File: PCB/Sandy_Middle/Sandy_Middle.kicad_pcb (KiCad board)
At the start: 2 copper layers, 285 x 75.2 mm, 134 parts, among them J1 Conn_02x02_Top_Bottom, J2 Conn_02x02_Top_Bottom, J3 Conn_02x02_Top_Bottom

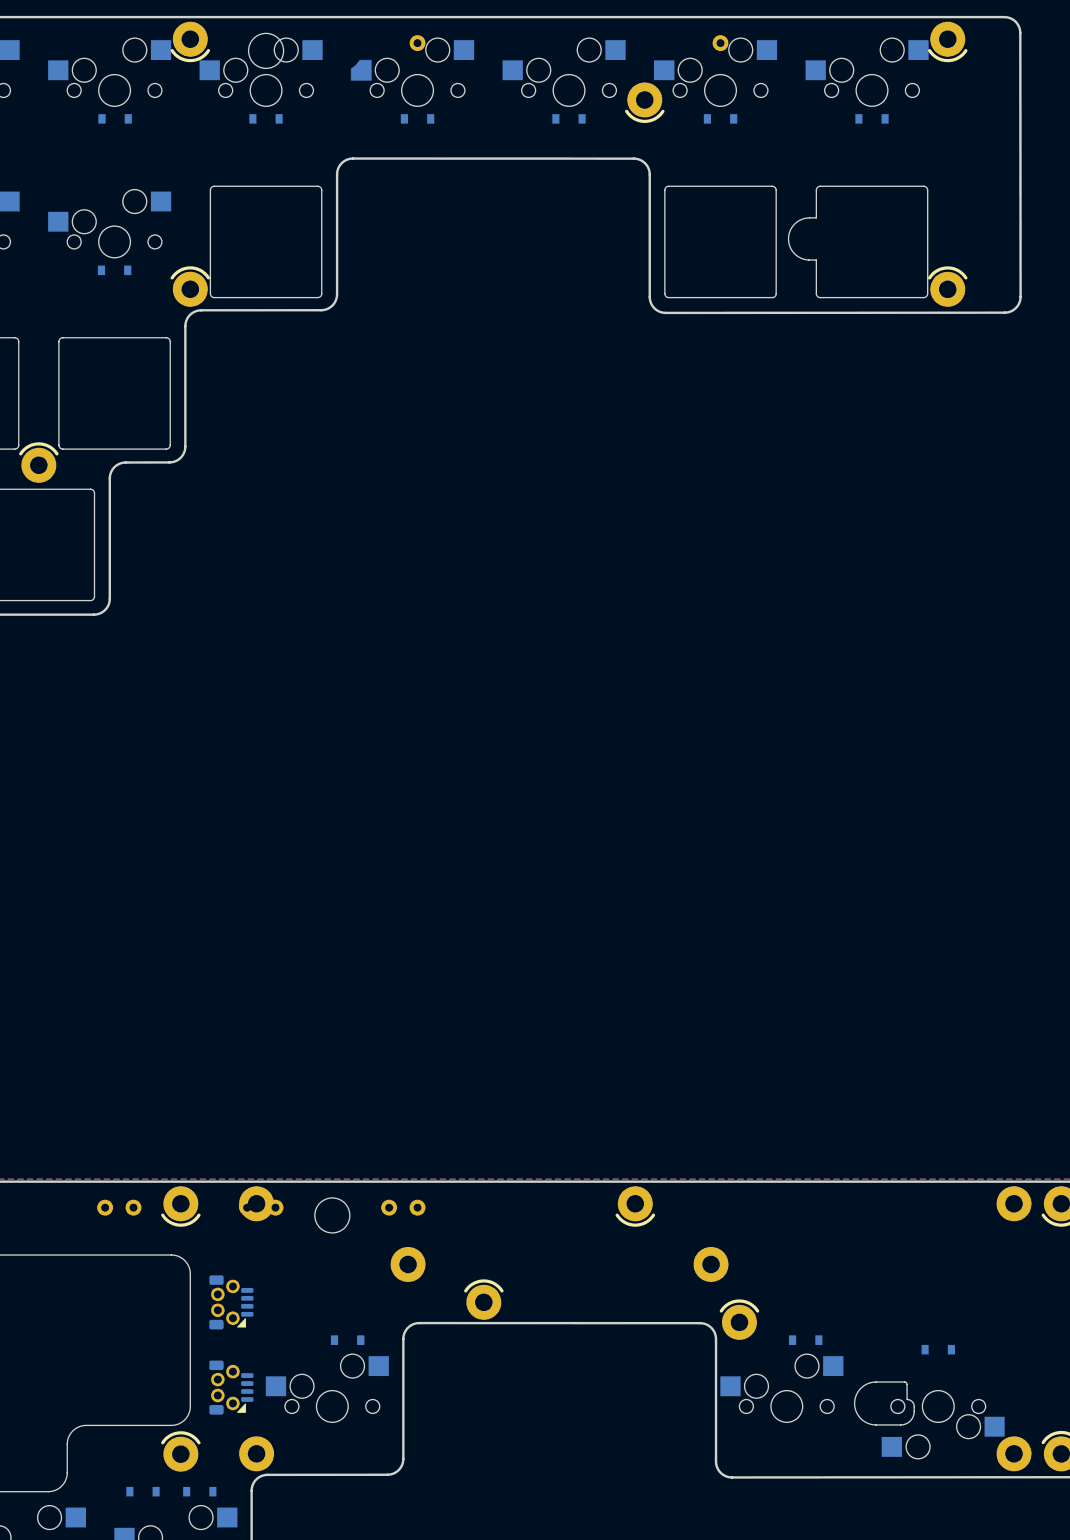
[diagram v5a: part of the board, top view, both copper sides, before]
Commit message: スイッチの配置イメージをDN0040レイアウトに変更
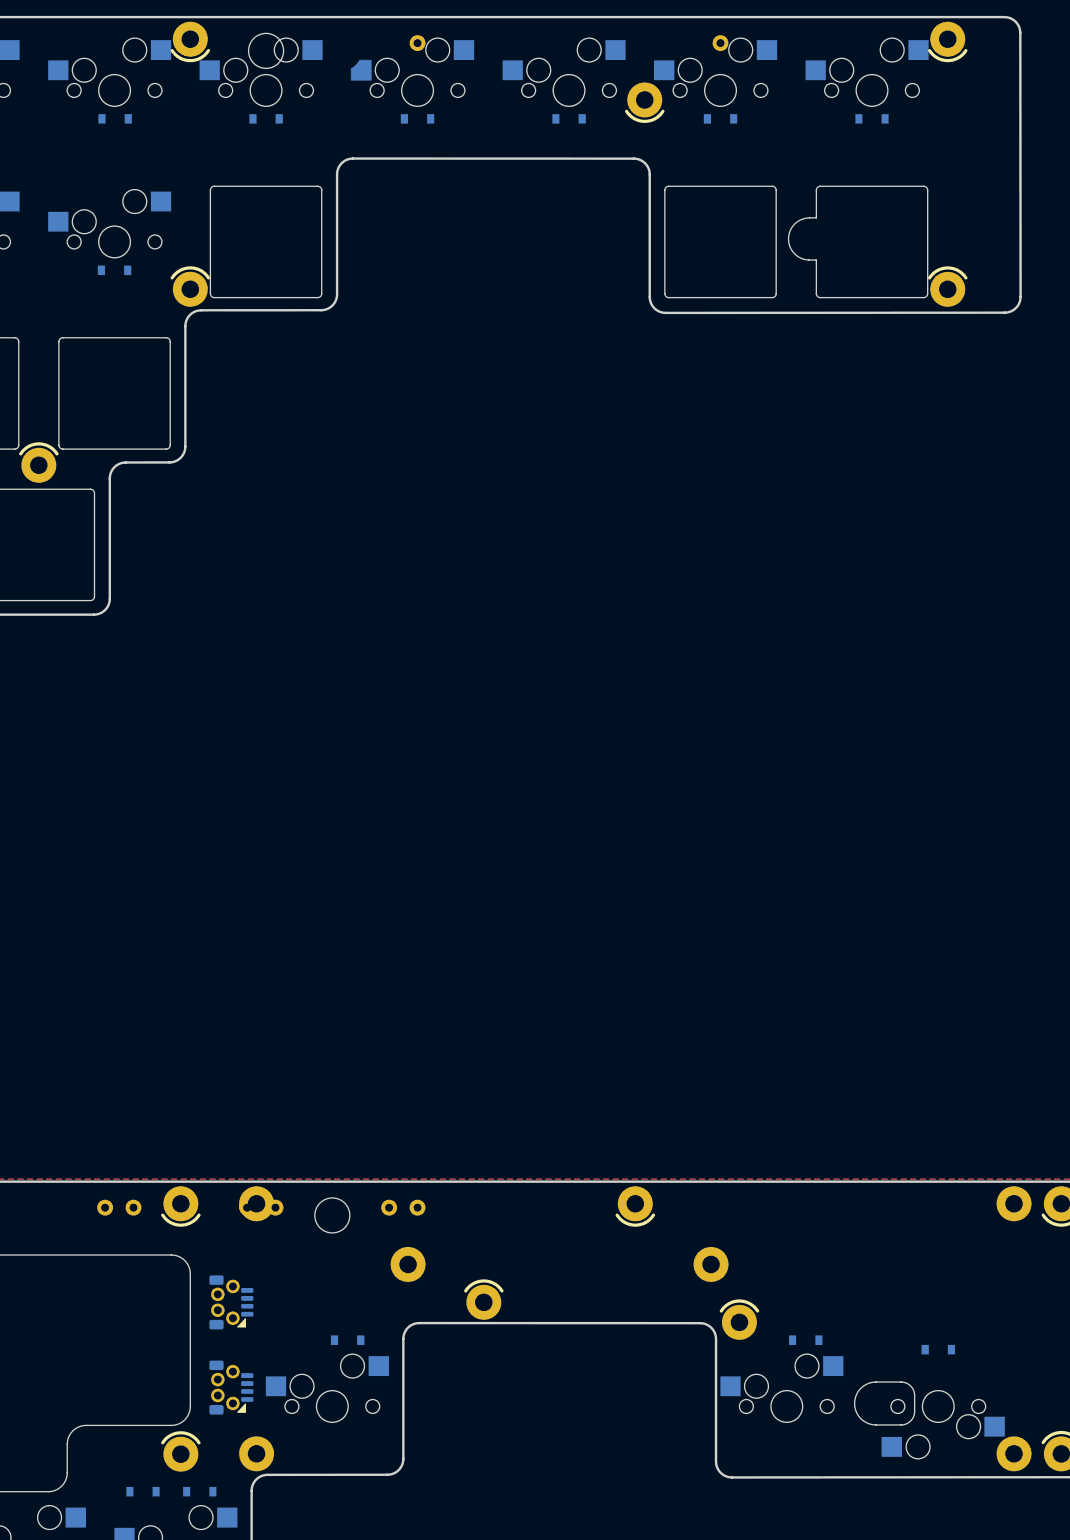
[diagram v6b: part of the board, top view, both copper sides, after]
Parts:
- Cutout1: footprint locallib:60_Outline-Sandy-Mid7-narrow-bottom-small-right-hole -> locallib:60_Outline-Sandy-DN0040-Mid
- REF**: footprint locallib:60_Outline-Sandy-Top-NoSwImage-WithHole2-ECO1 -> locallib:60_Outline-Sandy-DN0040-Top-NoSwImage-WithHole2-ECO1

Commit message: ネジ穴と接続するピンを調整中
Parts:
- removed ?: , clipboard:1d23b097-72e0-487b-bec7-a328ee8b6ed7
- removed the D1 at (31.8, -112.3)
- removed D10 (x2), D14, D16, D17, D18, D19, D8 (x2): D, locallib:D_SOD-123_Emphasized_Direction_Line
- removed the D11 at (222.3, -112.3)
- removed the D12 at (241.3, -112.3)
- removed the D13 at (260.4, -112.3)
- removed the D2 at (50.8, -112.3)
- removed the D3 at (69.9, -112.3)
- removed the D4 at (88.9, -112.3)
- removed the D5 at (108.0, -112.3)
- removed the D6 at (127.0, -112.3)
- removed the D7 at (146.1, -112.3)
- removed the D9 at (184.2, -112.3)
- removed EXT_TC0, EXT_TC1, EXT_TC2, EXT_TC3, EXT_TC4, EXT_TC5, EXT_TC6, EXT_TR0, EXT_TR1, EXT_TR5, EXT_TR6: Conn_01x01, TestPoint:TestPoint_THTPad_D2.0mm_Drill1.0mm
- removed the H1 at (22.2, -122.3)
- removed the H10 at (288.9, -90.9)
- removed the H11 at (136.5, -68.7)
- removed the H12 at (174.6, -68.7)
- removed the H2 at (117.5, -122.3)
- removed the H3 at (193.7, -122.3)
- removed the H4 at (288.9, -122.3)
- removed the H5 at (22.2, -90.9)
- removed the H6 at (60.3, -114.7)
- removed the H7 at (117.5, -90.9)
- removed the H8 at (193.7, -90.9)
- removed the H9 at (250.8, -114.7)
- removed the J1 at (165.1, -113.3)
- removed the J2 at (146.1, -113.3)
- removed the J3 at (129.4, -109.9)
- removed the REF** at (155.6, -87.3)
- removed SW_-1: SW_Push, MX_Alps_Hybrid:MXOnly-1U-Hotswap-screw-hole-side1-guide
- removed SW_1, SW_10, SW_2, SW_3, SW_4, SW_6, SW_7, SW_9, SW_;1, SW_=1, SW_ESC1, SW_INS1, SW_T1, SW_Y1, SW_[1, SW_]1: SW_Push, MX_Alps_Hybrid:MXOnly-1U-Hotswap-guide
- removed SW_5: SW_Push, MX_Alps_Hybrid:MXOnly-1U-Hotswap-screw-hole-side2-guide
- removed SW_8: SW_Push, MX_Alps_Hybrid:MXOnly-1U-Hotswap-screw-hole-side3-guide
- removed the SW_H1 at (192.5, 68.7)
- added EXT_MC1: Conn_01x01, TestPoint:TestPoint_THTPad_D2.0mm_Drill1.0mm, B.Cu at (243.7, 66.1)
- added EXT_MC5: Conn_01x01, TestPoint:TestPoint_THTPad_D2.0mm_Drill1.0mm, B.Cu at (243.7, 70.1)
- added EXT_MR0: Conn_01x01, TestPoint:TestPoint_THTPad_D2.0mm_Drill1.0mm, B.Cu at (243.7, 74.2)
- added EXT_MR5: Conn_01x01, TestPoint:TestPoint_THTPad_D2.0mm_Drill1.0mm, B.Cu at (243.7, 78.2)
- added H_top_13: MountingHole, locallib:MountingHole_2.2mm_M2_Pad_minimal, F.Cu at (163.9, 77.7)
- H15, H16: moved to B.Cu
- moved SW_H1 19.0 mm to (192.5, 68.7)
- turned H15 to 180 degrees
- turned H16 to 180 degrees
- renumbered SW_'1 to SW_H1
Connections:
- H_top_1 pad 1: unconnected-(H_top_1-Pad1) -> Top_col0
- H_top_10 pad 1: unconnected-(H_top_10-Pad1) -> Top_row5
- H_top_11 pad 1: unconnected-(H_top_11-Pad1) -> Top_col3
- H_top_12 pad 1: unconnected-(H_top_12-Pad1) -> Top_row2
- H_top_2 pad 1: unconnected-(H_top_2-Pad1) -> Top_col2
- H_top_3 pad 1: unconnected-(H_top_3-Pad1) -> Top_col4
- H_top_4 pad 1: unconnected-(H_top_4-Pad1) -> Top_col6
- H_top_5 pad 1: unconnected-(H_top_5-Pad1) -> Top_row0
- H_top_6 pad 1: unconnected-(H_top_6-Pad1) -> Top_col1
- H_top_7 pad 1: unconnected-(H_top_7-Pad1) -> Top_row1
- H_top_8 pad 1: unconnected-(H_top_8-Pad1) -> Top_row6
- H_top_9 pad 1: unconnected-(H_top_9-Pad1) -> Top_col5
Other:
- board size 285 x 75.2 mm -> 285 x 73.4 mm
- board text removed: "#Sandy_kbd DN0030, Top & Plate for Mid by @jpskenn"
- board text removed: "Top 1"
- board text removed: "Top 2"
- board text removed: "Top 3"
- board text removed: "to Mid"

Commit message: ネジ穴と接続するピンを調整中
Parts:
- added ?: , clipboard:1d23b097-72e0-487b-bec7-a328ee8b6ed7, F.Cu at (147.2, -36.6)
- added D1: D, locallib:D_SOD-123_Emphasized_Direction_Line, B.Cu at (40.1, -56.8)
- added D10: D, locallib:D_SOD-123_Emphasized_Direction_Line, B.Cu at (211.6, -56.8)
- added D11: D, locallib:D_SOD-123_Emphasized_Direction_Line, B.Cu at (230.6, -56.8)
- added D12: D, locallib:D_SOD-123_Emphasized_Direction_Line, B.Cu at (249.7, -56.8)
- added D13: D, locallib:D_SOD-123_Emphasized_Direction_Line, B.Cu at (268.7, -56.8)
- added D14: D, locallib:D_SOD-123_Emphasized_Direction_Line, B.Cu at (287.8, -56.8)
- added D15: D, locallib:D_SOD-123_Emphasized_Direction_Line, B.Cu at (154.3, -18.7)
- added D16: D, locallib:D_SOD-123_Emphasized_Direction_Line, B.Cu at (135.4, -37.8)
- added D17: D, locallib:D_SOD-123_Emphasized_Direction_Line, B.Cu at (154.4, -37.8)
- added D18: D, locallib:D_SOD-123_Emphasized_Direction_Line, B.Cu at (173.5, -37.8)
- added D19: D, locallib:D_SOD-123_Emphasized_Direction_Line, B.Cu at (192.5, -37.8)
- added D2: D, locallib:D_SOD-123_Emphasized_Direction_Line, B.Cu at (59.2, -56.8)
- added D20: D, locallib:D_SOD-123_Emphasized_Direction_Line, B.Cu at (173.5, -18.7)
- added D3: D, locallib:D_SOD-123_Emphasized_Direction_Line, B.Cu at (78.2, -56.8)
- added D4: D, locallib:D_SOD-123_Emphasized_Direction_Line, B.Cu at (97.3, -56.8)
- added D5: D, locallib:D_SOD-123_Emphasized_Direction_Line, B.Cu at (116.3, -56.8)
- added D6: D, locallib:D_SOD-123_Emphasized_Direction_Line, B.Cu at (135.4, -56.8)
- added D7: D, locallib:D_SOD-123_Emphasized_Direction_Line, B.Cu at (154.4, -56.8)
- added D8: D, locallib:D_SOD-123_Emphasized_Direction_Line, B.Cu at (173.5, -56.8)
- added D9: D, locallib:D_SOD-123_Emphasized_Direction_Line, B.Cu at (192.6, -56.8)
- added EXT_TC0: Conn_01x01, TestPoint:TestPoint_THTPad_D2.0mm_Drill1.0mm, B.Cu at (49.6, -66.4)
- added EXT_TC1: Conn_01x01, TestPoint:TestPoint_THTPad_D2.0mm_Drill1.0mm, B.Cu at (87.7, -66.4)
- added EXT_TC2: Conn_01x01, TestPoint:TestPoint_THTPad_D2.0mm_Drill1.0mm, B.Cu at (106.8, -66.4)
- added EXT_TC3: Conn_01x01, TestPoint:TestPoint_THTPad_D2.0mm_Drill1.0mm, B.Cu at (163.9, -66.4)
- added EXT_TC4: Conn_01x01, TestPoint:TestPoint_THTPad_D2.0mm_Drill1.0mm, B.Cu at (183.0, -66.4)
- added EXT_TC5: Conn_01x01, TestPoint:TestPoint_THTPad_D2.0mm_Drill1.0mm, B.Cu at (240.1, -66.4)
- added EXT_TC6: Conn_01x01, TestPoint:TestPoint_THTPad_D2.0mm_Drill1.0mm, B.Cu at (278.2, -66.4)
- added EXT_TR0: Conn_01x01, TestPoint:TestPoint_THTPad_D2.0mm_Drill1.0mm, B.Cu at (30.6, -56.8)
- added EXT_TR1: Conn_01x01, TestPoint:TestPoint_THTPad_D2.0mm_Drill1.0mm, B.Cu at (148.5, -37.8)
- added EXT_TR2: Conn_01x01, TestPoint:TestPoint_THTPad_D2.0mm_Drill1.0mm, B.Cu at (148.5, -30.6)
- added EXT_TR5: Conn_01x01, TestPoint:TestPoint_THTPad_D2.0mm_Drill1.0mm, B.Cu at (30.6, -53.3)
- added EXT_TR6: Conn_01x01, TestPoint:TestPoint_THTPad_D2.0mm_Drill1.0mm, B.Cu at (148.5, -34.2)
- added H1: MountingHole, locallib:MountingHole_2.2mm_M2_Pad_minimal, F.Cu at (30.6, -66.8)
- added H10: MountingHole, locallib:MountingHole_2.2mm_M2_Pad_minimal, F.Cu at (297.3, -35.4)
- added H11: MountingHole, locallib:MountingHole_2.2mm_M2_Pad_minimal, F.Cu at (30.6, -35.4)
- added H12: MountingHole, locallib:MountingHole_2.2mm_M2_Pad_minimal, F.Cu at (125.8, -35.4)
- added H13: MountingHole, locallib:MountingHole_2.2mm_M2_Pad_minimal, F.Cu at (163.9, -13.3)
- added H2: MountingHole, locallib:MountingHole_2.2mm_M2_Pad_minimal, F.Cu at (125.8, -66.8)
- added H3: MountingHole, locallib:MountingHole_2.2mm_M2_Pad_minimal, F.Cu at (202.0, -66.8)
- added H4: MountingHole, locallib:MountingHole_2.2mm_M2_Pad_minimal, F.Cu at (297.3, -66.8)
- added H5: MountingHole, locallib:MountingHole_2.2mm_M2_Pad_minimal, F.Cu at (68.7, -59.2)
- added H6: MountingHole, locallib:MountingHole_2.2mm_M2_Pad_minimal, F.Cu at (106.8, -59.2)
- added H7: MountingHole, locallib:MountingHole_2.2mm_M2_Pad_minimal, F.Cu at (221.1, -59.2)
- added H8: MountingHole, locallib:MountingHole_2.2mm_M2_Pad_minimal, F.Cu at (259.2, -59.2)
- added H9: MountingHole, locallib:MountingHole_2.2mm_M2_Pad_minimal, F.Cu at (202.0, -35.4)
- added J1: Conn_02x02_Top_Bottom, locallib:JST_SH_SM04B-SRSS-TB_1x04-1MP_P1.00mm_Horizontal_wCable_housing_spare_pin, B.Cu at (183.0, -57.8)
- added J2: Conn_02x02_Top_Bottom, locallib:JST_SH_SM04B-SRSS-TB_1x04-1MP_P1.00mm_Horizontal_wCable_housing_spare_pin, B.Cu at (163.9, -57.8)
- added J3: Conn_02x02_Top_Bottom, locallib:JST_SH_SM04B-SRSS-TB_1x04-1MP_P1.00mm_Horizontal_wCable_housing_spare_pin, B.Cu at (142.1, -54.4)
- added REF**: 60_Outline, locallib:60_Outline-Sandy-DN0040-Top, F.Cu at (163.9, -31.8)
- added SW_'1: SW_Push, MX_Alps_Hybrid:MXOnly-1U-Hotswap-guide, F.Cu at (173.5, -22.3)
- added SW_-1: SW_Push, MX_Alps_Hybrid:MXOnly-1U-Hotswap-screw-hole-side1-guide, F.Cu at (154.4, -60.4)
- added SW_1: SW_Push, MX_Alps_Hybrid:MXOnly-1U-Hotswap-guide, F.Cu at (59.2, -60.4)
- added SW_10: SW_Push, MX_Alps_Hybrid:MXOnly-1U-Hotswap-guide, F.Cu at (268.7, -60.4)
- added SW_2: SW_Push, MX_Alps_Hybrid:MXOnly-1U-Hotswap-guide, F.Cu at (78.2, -60.4)
- added SW_3: SW_Push, MX_Alps_Hybrid:MXOnly-1U-Hotswap-guide, F.Cu at (97.3, -60.4)
- added SW_4: SW_Push, MX_Alps_Hybrid:MXOnly-1U-Hotswap-guide, F.Cu at (116.3, -60.4)
- added SW_5: SW_Push, MX_Alps_Hybrid:MXOnly-1U-Hotswap-screw-hole-side2-guide, F.Cu at (135.4, -60.4)
- added SW_6: SW_Push, MX_Alps_Hybrid:MXOnly-1U-Hotswap-guide, F.Cu at (192.5, -60.4)
- added SW_7: SW_Push, MX_Alps_Hybrid:MXOnly-1U-Hotswap-guide, F.Cu at (211.6, -60.4)
- added SW_8: SW_Push, MX_Alps_Hybrid:MXOnly-1U-Hotswap-screw-hole-side3-guide, F.Cu at (230.6, -60.4)
- added SW_9: SW_Push, MX_Alps_Hybrid:MXOnly-1U-Hotswap-guide, F.Cu at (249.7, -60.4)
- added SW_;1: SW_Push, MX_Alps_Hybrid:MXOnly-1U-Hotswap-guide, F.Cu at (154.4, -22.3)
- added SW_=1: SW_Push, MX_Alps_Hybrid:MXOnly-1U-Hotswap-guide, F.Cu at (173.5, -60.4)
- added SW_ESC1: SW_Push, MX_Alps_Hybrid:MXOnly-1U-Hotswap-guide, F.Cu at (40.1, -60.4)
- added SW_INS1: SW_Push, MX_Alps_Hybrid:MXOnly-1U-Hotswap-guide, F.Cu at (287.8, -60.4)
- added SW_T1: SW_Push, MX_Alps_Hybrid:MXOnly-1U-Hotswap-guide, F.Cu at (135.4, -41.4)
- added SW_Y1: SW_Push, MX_Alps_Hybrid:MXOnly-1U-Hotswap-guide, F.Cu at (192.5, -41.4)
- added SW_[1: SW_Push, MX_Alps_Hybrid:MXOnly-1U-Hotswap-guide, F.Cu at (154.4, -41.4)
- added SW_]1: SW_Push, MX_Alps_Hybrid:MXOnly-1U-Hotswap-guide, F.Cu at (173.5, -41.4)
- H15, H16: moved to F.Cu
- H_top_13: moved to B.Cu
- moved EXT_MR0 219.0 mm to (28.2, 35.3)
- moved EXT_MC1 186.8 mm to (61.5, 24.6)
- moved EXT_MR5 56.6 mm to (258.0, 23.4)
- moved EXT_MC5 48.9 mm to (225.8, 24.6)
- moved EXT_MR6 28.3 mm to (28.2, 44.9)
- moved EXT_MR1 21.6 mm to (28.2, 40.1)
- moved EXT_MR2 3.57 mm to (208.0, 24.6)
- turned H15 to 0 degrees
- turned H16 to 0 degrees
- turned H_top_13 to 180 degrees
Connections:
- H1 pad 1: unconnected-(H1-Pad1) -> Mid_col0
- H10 pad 1: unconnected-(H10-Pad1) -> Mid_row5
- H11 pad 1: unconnected-(H11-Pad1) -> Mid_row0
- H12 pad 1: unconnected-(H12-Pad1) -> Mid_GND
- H13 pad 1: unconnected-(H13-Pad1) -> Mid_row2
- H14 pad 1: unconnected-(H14-Pad1) -> Mid_row7
- H15 pad 1: unconnected-(H15-Pad1) -> Mid_row3
- H16 pad 1: unconnected-(H16-Pad1) -> Mid_row8
- H2 pad 1: unconnected-(H2-Pad1) -> Mid_row1
- H3 pad 1: unconnected-(H3-Pad1) -> Mid_col3
- H4 pad 1: unconnected-(H4-Pad1) -> Mid_col4
- H5 pad 1: unconnected-(H5-Pad1) -> Mid_row6
- H6 pad 1: unconnected-(H6-Pad1) -> Mid_col6
- H7 pad 1: unconnected-(H7-Pad1) -> Mid_col2
- H8 pad 1: unconnected-(H8-Pad1) -> Mid_col5
- H9 pad 1: unconnected-(H9-Pad1) -> Mid_col1
- H_top_1 pad 1: Top_col0 -> Mid_col0
- H_top_10 pad 1: Top_row5 -> Mid_GND
- H_top_11 pad 1: Top_col3 -> Mid_row1
- H_top_12 pad 1: Top_row2 -> Mid_row6
- H_top_13 pad 1: Top_GND -> Mid_row2
- H_top_2 pad 1: Top_col2 -> Mid_col3
- H_top_3 pad 1: Top_col4 -> Mid_col4
- H_top_4 pad 1: Top_col6 -> Mid_col6
- H_top_5 pad 1: Top_row0 -> Mid_row0
- H_top_6 pad 1: Top_col1 -> Mid_col1
- H_top_7 pad 1: Top_row1 -> Mid_col2
- H_top_8 pad 1: Top_row6 -> Mid_col5
- H_top_9 pad 1: Top_col5 -> Mid_row5
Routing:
- net Top_col0: track 0.00 -> 29.2 mm
- added copper zone on B.Cu, net Mid_row6
- added copper zone on F.Cu, net Mid_row6
- removed copper zone on B.Cu, net unconnected-(H5-Pad1)
- removed copper zone on F.Cu, net unconnected-(H5-Pad1)
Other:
- board size 285 x 73.4 mm -> 285 x 75.2 mm
- board text added: "#Sandy_kbd DN0040, Top & Plate for Mid by @jpskenn"
- board text added: "Top 1"
- board text added: "Top 2"
- board text added: "Top 3"
- board text added: "to Mid"
